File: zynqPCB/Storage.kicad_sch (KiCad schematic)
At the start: 22 parts, among them J8 Micro_SD_Card_Det, U17 FTDITypeUART, U18 ABRACON-ASDMB, U19 S25FL256SAGNFI001, U20F xc7z020clg484

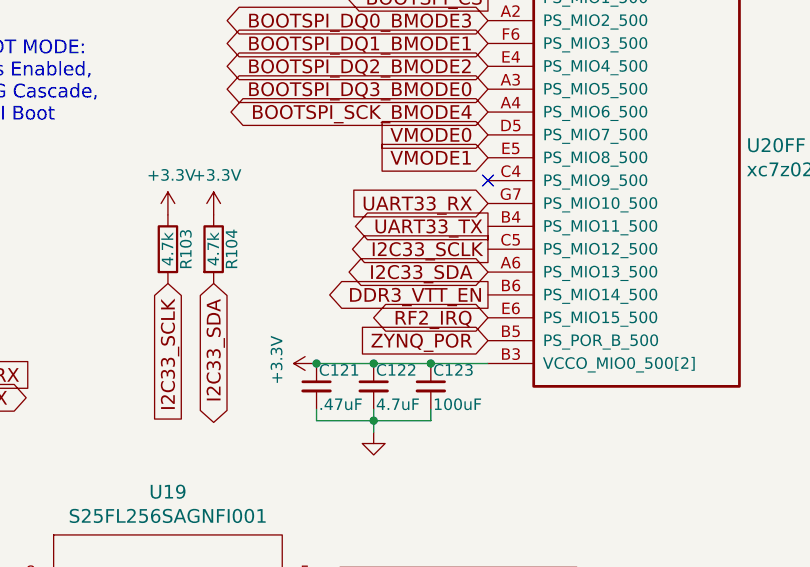
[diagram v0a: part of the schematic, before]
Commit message: Remove Sensors
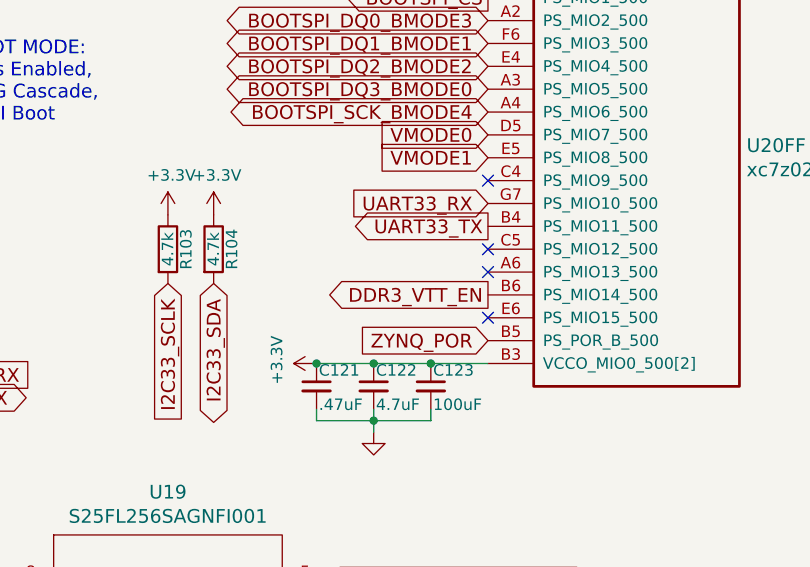
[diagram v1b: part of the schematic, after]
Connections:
- net I2C33_SCLK: no longer U20F.C5 (PS_MIO12_500)
- net I2C33_SDA: no longer U20F.A6 (PS_MIO13_500)
- net RF2_IRQ: no longer names the net of U20F.E6 (PS_MIO15_500)
- no-connect marks 4 -> 7
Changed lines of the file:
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@@
+	)
+	(no_connect
+		(at 207.01 102.87)
 	)
 	(no_connect
@@
 	(no_connect
 		(at 140.97 114.3)
+	)
+	(no_connect
+		(at 207.01 95.25)
+	)
+	(no_connect
+		(at 207.01 97.79)
 	)
 	(wire
@@
 		)
 	)
-	(global_label "I2C33_SDA"
-		(shape bidirectional)
-		(at 207.01 97.79 180)
-		(effects
-			(font
-				(size 1.524 1.524)
-			)
-			(justify right)
-		)
-		(property "Intersheetrefs" "${INTERSHEET_REFS}"
-			(at 207.01 97.79 0)
-			(effects
-				(font
-					(size 1.27 1.27)
-				)
-				(hide yes)
-			)
-		)
-	)
 	(global_label "BOOTSPI_DQ3_BMODE0"
 		(shape bidirectional)
@@
 		(property "Intersheetrefs" "${INTERSHEET_REFS}"
 			(at 189.23 139.7 0)
-			(effects
-				(font
-					(size 1.27 1.27)
-				)
-				(hide yes)
-			)
-		)
-	)
-	(global_label "I2C33_SCLK"
-		(shape output)
-		(at 207.01 95.25 180)
-		(effects
-			(font
-				(size 1.524 1.524)
-			)
-			(justify right)
-		)
-		(property "Intersheetrefs" "${INTERSHEET_REFS}"
-			(at 207.01 95.25 0)
 			(effects
 				(font
@@
 			(effects
 				(font
-					(size 1.27 1.27)
-				)
-				(hide yes)
-			)
-		)
-	)
-	(global_label "RF2_IRQ"
-		(shape bidirectional)
-		(at 207.01 102.87 180)
-		(effects
-			(font
-				(size 1.524 1.524)
-			)
-			(justify right)
-		)
-		(property "Intersheetrefs" "${INTERSHEET_REFS}"
-			(at 207.01 102.87 0)
-			(effects
-				(font
